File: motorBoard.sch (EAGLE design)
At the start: 8 parts, among them U1 CY8C4247AZI-L485TQFN

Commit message: PRR
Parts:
- removed LED1: (no value), eagle-ltspice:LED_ESML0603
- removed SV1: (no value), con-amp-mt:L05P
- removed SV2: (no value), con-amp-mt:L04P
- added ENCD1, ENCD2, ENCD3, ENCD4: MOLEX5, HuskyRobotics2017-18:MOLEX5
- added LED2: (no value), eagle-ltspice:LED_E
- added LIMIT4A, LIMIT4A1, LIMIT4A2, LIMIT4A3, LIMIT4B, LIMIT4B1, LIMIT4B2, LIMIT4B3, POT1, POT2, POT3, POT4, PWM1, PWM2, PWM3, PWM4: MOLEX3, HuskyRobotics2017-18:MOLEX3
- added U$5: OKI-78SR-3.33SIP, HuskyRobotics2017-18:OKI-78SR-3.33SIP
- added U$6, U$7, U$8, U$9: LEVEL-SHIFTER_NVT2003DPNVT_2003DP_LEVEL_SHIFTER, HuskyRobotics2017-18:LEVEL-SHIFTER_NVT2003DPNVT_2003DP_LEVEL_SHIFTER
- U$2: value OKI-78SR3SIP -> OKI-78SR-53SIP; device HuskyRobotics2017-18:OKI-78SR3SIP -> HuskyRobotics2017-18:OKI-78SR-53SIP
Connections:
- removed net B$10: SV1-1.S, SV1-2.S, SV1-3.S, U1.P3.1, U1.P3.2, U1.P3.3
- removed net B$11: SV2-1.S, SV2-2.S, U1.P3.4, U1.P3.5
- removed net B$2: U1.P0.1, U1.P0.2
- removed net B$6: U1.P1.1, U1.P1.2, U1.P1.3
- removed net B$7: U1.P1.4, U1.P1.5
- removed net B$8: U1.P2.1, U1.P2.2, U1.P2.3
- removed net B$9: U1.P2.4, U1.P2.5
- removed net N$12: SV2-4.S, U$1.VCC, U$2.OUTPUT+, U$3.1A, U$3.2A, U$3.3A, U$3.4A, U$4.OUT_EN, U$4.VCC, U1.VCCD, U1.VDDA@11, U1.VDDA@56, U1.VDDD, U1.VDDIO
- removed net N$13: SV1-4.S, SV1-5.S, SV2-3.S, U$1.GND, U$2.GND, U$4.GND, U1.VSSA@10, U1.VSSA@57, U1.VSSD, U1.VSSIO
- new net +3V3: LIMIT4A.1, LIMIT4A1.1, LIMIT4A2.1, LIMIT4A3.1, LIMIT4B.1, LIMIT4B1.1, LIMIT4B2.1, LIMIT4B3.1, PWM1.1, PWM2.1, PWM3.1, PWM4.1, U$3.1A, U$3.2A, U$3.3A, U$3.4A, U$4.OUT_EN, U$4.VCC, U$5.OUTPUT+, U$6.AREF, U$7.AREF, U$8.AREF, U$9.AREF, U1.VCCD, U1.VDDD, U1.VDDIO
- new net +5V: ENCD1.1, ENCD2.1, ENCD3.1, ENCD4.1, POT1.1, POT2.1, POT3.1, POT4.1, U$2.OUTPUT+, U1.VDDA@11, U1.VDDA@56
- new net GNDA: ENCD1.2, ENCD2.2, ENCD3.2, ENCD4.2, LIMIT4A.2, LIMIT4A1.2, LIMIT4A2.2, LIMIT4A3.2, LIMIT4B.2, LIMIT4B1.2, LIMIT4B2.2, LIMIT4B3.2, POT1.2, POT2.2, POT3.2, POT4.2, PWM1.2, PWM2.2, PWM3.2, PWM4.2, U$2.GND, U$4.GND, U$5.GND, U$6.GND, U$7.GND, U$8.GND, U$9.GND, U1.VSSA@10, U1.VSSA@57, U1.VSSD, U1.VSSIO
- new net N$10: ENCD4.3, U$6.B3
- new net N$11: ENCD4.4, U$6.B2
- new net N$16: ENCD4.5, U$6.B1
- new net N$17: PWM1.3, U1.P2.0
- new net N$18: POT4.3, U1.P3.6
- new net N$19: LIMIT4B.3, U1.P3.5
- new net N$20: LIMIT4A.3, U1.P3.4
- new net N$21: U$7.BREF, U$7.EN
- new net N$22: U$7.A3, U1.P2.1
- new net N$23: U$7.A2, U1.P2.2
- new net N$24: U$7.A1, U1.P2.3
- new net N$25: ENCD1.3, U$7.B3
- new net N$26: ENCD1.4, U$7.B2
- new net N$27: ENCD1.5, U$7.B1
- new net N$28: LIMIT4B1.3, U1.P2.5
- new net N$29: LIMIT4A1.3, U1.P2.4
- new net N$30: POT1.3, U1.P2.6
- new net N$31: PWM2.3, U1.P1.0
- new net N$32: U$8.BREF, U$8.EN
- new net N$33: U$8.A3, U1.P1.1
- new net N$34: U$8.A2, U1.P1.2
- new net N$35: U$8.A1, U1.P1.3
- new net N$36: ENCD2.3, U$8.B3
- new net N$37: ENCD2.4, U$8.B2
- new net N$38: ENCD2.5, U$8.B1
- new net N$39: LIMIT4B2.3, U1.P1.5
- new net N$40: LIMIT4A2.3, U1.P1.4
- new net N$41: POT2.3, U1.P1.6
- new net N$42: PWM3.3, U1.P0.0
- new net N$43: U$9.BREF, U$9.EN
- new net N$44: U$9.A3, U1.P0.1
- new net N$45: U$9.A2, U1.P0.2
- new net N$46: U$9.A1, U1.P0.3
- new net N$47: ENCD3.3, U$9.B3
- new net N$48: ENCD3.4, U$9.B2
- new net N$49: ENCD3.5, U$9.B1
- new net N$50: LIMIT4B3.3, U1.P0.5
- new net N$51: LIMIT4A3.3, U1.P0.4
- new net N$52: POT3.3, U1.P0.6
- net B$4: now also U$3.1B, U$3.4B; no longer U1.P5.1, U1.P5.2
- net N$14: now also U$5.INPUT+
- net N$3: now also U$6.BREF, U$6.EN; no longer U1.P0.0
- net N$4: now also U$3.2B, U1.P5.1; no longer U1.P1.0
- net N$5: now also U$3.3B, U1.P5.2; no longer U1.P2.0
- net N$6: now also PWM4.3
- net N$7: now also U$6.A3, U1.P3.1; no longer U1.P0.5
- net N$8: now also U$6.A2, U1.P3.2; no longer U1.P0.4
- net N$9: now also U$6.A1, U1.P3.3; no longer U1.P0.3
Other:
- note removed: "Each motor has 3 encoder or 1 analog input, 2 limit switches, and 1 pwm output. Analog or Encoder mode is controlled by DIP switch."
- note removed: "LEDs can be connected to some odd GPIOs"
- note removed: "Motor 1 Encoder Inputs"
- note removed: "Motor 1 Limit Switches"
- note removed: "Motor 2 Encoder Inputs"
- note removed: "Motor 2 Limit Switches"
- note removed: "Motor 2 PWM"
- note removed: "Motor 3 Encoder Inputs"
- note removed: "Motor 3 Limit Switches"
- note removed: "Motor 3 PWM"
- note removed: "Motor 4 Encoder Inputs"
- note removed: "Motor 4 Limit Switches"
- note removed: "Motor 4 PWM"
- note removed: "PWM"

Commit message: Minor Tweaks
Added a couple of ground and voltage references.
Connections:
- net +3V3: now also U$1.VCC
- net GNDA: now also U$1.GND
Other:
- moved on the sheet: ENCD4, LIMIT4A, LIMIT4B, POT4, PWM4, U$2, U$5

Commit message: Finishing touches on the schematic
Added indicator LEDs, labeled all nets, spare gpio headers, cleaned up schematic, other misc.  Quickie layout and auto router just for funsies.
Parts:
- removed ENCD1, ENCD2, ENCD3, ENCD4: MOLEX5, HuskyRobotics2017-18:MOLEX5
- removed LIMIT4A, LIMIT4A1, LIMIT4A2, LIMIT4A3, LIMIT4B, LIMIT4B1, LIMIT4B2, LIMIT4B3: MOLEX3, HuskyRobotics2017-18:MOLEX3
- removed U$2: OKI-78SR-53SIP, HuskyRobotics2017-18:OKI-78SR-53SIP
- removed U$5: OKI-78SR-3.33SIP, HuskyRobotics2017-18:OKI-78SR-3.33SIP
- added 1_ENCD3V3, 1_ENCD5V, 2_ENCD3V3, 2_ENCD5V, 3_ENCD3V3, 3_ENCD5V, 4_ENCD3V3, 4_ENCD5V: MOLEX5, HuskyRobotics2017-18:MOLEX5
- added BASIC_HEADER: 2BASIC_HEADER, HuskyRobotics2017-18:2BASIC_HEADER
- added BASIC_HEADER1, BASIC_HEADER2: 6BASIC_HEADER, HuskyRobotics2017-18:6BASIC_HEADER
- added LED1, LED3, LED4, LED5, LED6, LED7, LED8: (no value), eagle-ltspice:LED_E
- added LIMITA1, LIMITA2, LIMITA3, LIMITA4, LIMITB1, LIMITB2, LIMITB3, LIMITB4: MOLEX3, HuskyRobotics2017-18:MOLEX3
- added OKI-78SR-3.3: OKI-78SR-3.33SIP, HuskyRobotics2017-18:OKI-78SR-3.33SIP
- added OKI-78SR-5: OKI-78SR-53SIP, HuskyRobotics2017-18:OKI-78SR-53SIP
- added R1, R2, R3, R4, R5, R6, R7, R8: (no value), eagle-ltspice:RR1206
- added RA, RB, RC, RD: 4.7k, eagle-ltspice:RR1206
- added U$10: SMD4SWSMD4SW, HuskyRobotics2017-18:SMD4SWSMD4SW
- renumbered U$4 to OSCILLATOR_SG-646PCE, U1 to PSOC4200L
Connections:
- net N$1 renamed CANRX
- net N$15 renamed CLK
- net N$2 renamed CANTX
- net N$4 renamed SEL_SW2
- net N$5 renamed SEL_SW3
- removed net B$1: PSOC4200L.P4.1, PSOC4200L.P4.2, PSOC4200L.P4.3, PSOC4200L.P4.4, PSOC4200L.P4.5, PSOC4200L.P4.6
- removed net B$4: PSOC4200L.P5.0, PSOC4200L.P5.3, U$3.1B, U$3.4B
- removed net N$11: ENCD4.4, U$6.B2
- removed net N$14: U$2.INPUT+, U$5.INPUT+
- removed net N$16: ENCD4.5, U$6.B1
- removed net N$18: POT4.3, PSOC4200L.P3.6
- removed net N$19: LIMIT4B.3, PSOC4200L.P3.5
- removed net N$21: U$7.BREF, U$7.EN
- removed net N$22: PSOC4200L.P2.1, U$7.A3
- removed net N$24: PSOC4200L.P2.3, U$7.A1
- removed net N$25: ENCD1.3, U$7.B3
- removed net N$26: ENCD1.4, U$7.B2
- removed net N$27: ENCD1.5, U$7.B1
- removed net N$28: LIMIT4B1.3, PSOC4200L.P2.5
- removed net N$29: LIMIT4A1.3, PSOC4200L.P2.4
- removed net N$3: U$6.BREF, U$6.EN
- removed net N$30: POT1.3, PSOC4200L.P2.6
- removed net N$31: PSOC4200L.P1.0, PWM2.3
- removed net N$32: U$8.BREF, U$8.EN
- removed net N$33: PSOC4200L.P1.1, U$8.A3
- removed net N$34: PSOC4200L.P1.2, U$8.A2
- removed net N$35: PSOC4200L.P1.3, U$8.A1
- removed net N$36: ENCD2.3, U$8.B3
- removed net N$37: ENCD2.4, U$8.B2
- removed net N$38: ENCD2.5, U$8.B1
- removed net N$39: LIMIT4B2.3, PSOC4200L.P1.5
- removed net N$40: LIMIT4A2.3, PSOC4200L.P1.4
- removed net N$41: POT2.3, PSOC4200L.P1.6
- removed net N$42: PSOC4200L.P0.0, PWM3.3
- removed net N$43: U$9.BREF, U$9.EN
- removed net N$44: PSOC4200L.P0.1, U$9.A3
- removed net N$45: PSOC4200L.P0.2, U$9.A2
- removed net N$46: PSOC4200L.P0.3, U$9.A1
- removed net N$47: ENCD3.3, U$9.B3
- removed net N$48: ENCD3.4, U$9.B2
- removed net N$49: ENCD3.5, U$9.B1
- removed net N$50: LIMIT4B3.3, PSOC4200L.P0.5
- removed net N$51: LIMIT4A3.3, PSOC4200L.P0.4
- removed net N$52: POT3.3, PSOC4200L.P0.6
- removed net N$6: PSOC4200L.P3.0, PWM4.3
- removed net N$8: PSOC4200L.P3.2, U$6.A2
- removed net N$9: PSOC4200L.P3.3, U$6.A1
- new net +24V: LED1.A, OKI-78SR-3.3.INPUT+, OKI-78SR-5.INPUT+
- new net BASIC_HEADER1-1: BASIC_HEADER1.1, PSOC4200L.P4.1
- new net BASIC_HEADER1-2: BASIC_HEADER1.2, PSOC4200L.P4.2
- new net BASIC_HEADER1-3: BASIC_HEADER1.3, PSOC4200L.P4.3
- new net BASIC_HEADER1-4: BASIC_HEADER1.4, PSOC4200L.P4.4
- new net BASIC_HEADER1-5: BASIC_HEADER1.5, PSOC4200L.P4.5
- new net BASIC_HEADER1-6: BASIC_HEADER1.6, PSOC4200L.P4.6
- new net BASIC_HEADER2-1: BASIC_HEADER2.1, PSOC4200L.P5.5
- new net BASIC_HEADER2-2: BASIC_HEADER2.2, PSOC4200L.P6.0
- new net BASIC_HEADER2-3: BASIC_HEADER2.3, PSOC4200L.P6.4/P12.0
- new net BASIC_HEADER2-4: BASIC_HEADER2.4, PSOC4200L.P6.5/P12.1
- new net BASIC_HEADER2-5: BASIC_HEADER2.5, PSOC4200L.P7.0
- new net BASIC_HEADER2-6: BASIC_HEADER2.6, PSOC4200L.P7.1
- new net CANH: U$1.CANH
- new net CANL: U$1.CANL
- new net LED4: LED4.A, PSOC4200L.P1.7/VREF
- new net LED5: LED5.A, PSOC4200L.P0.7
- new net LED6: LED6.A, PSOC4200L.P4.0
- new net LED7: LED7.A, PSOC4200L.D-/P13.1
- new net LED8: LED8.A, PSOC4200L.VBUS/P13.2
- new net LEVEL_SHIFT_EN1: RD.2, U$10.1B, U$8.EN
- new net LEVEL_SHIFT_EN2: RC.2, U$10.2B, U$7.EN
- new net LEVEL_SHIFT_EN3: RB.2, U$10.3B, U$6.EN
- new net LEVEL_SHIFT_EN4: RA.2, U$10.4B, U$9.EN
- new net MOTOR1A1: 1_ENCD3V3.4, PSOC4200L.P0.2, U$8.A1
- new net MOTOR1A2: 1_ENCD3V3.3, PSOC4200L.P0.1, U$8.A2
- new net MOTOR1A3: 1_ENCD3V3.2, PSOC4200L.P0.0, U$8.A3
- new net MOTOR1B1: 1_ENCD5V.4, U$8.B1
- new net MOTOR1B2: 1_ENCD5V.3, U$8.B2
- new net MOTOR1B3: 1_ENCD5V.2, U$8.B3
- new net MOTOR1LIMA: LIMITA1.2, PSOC4200L.P0.3
- new net MOTOR1LIMB: LIMITB1.2, PSOC4200L.P0.4
- new net MOTOR1POT: POT1.2, PSOC4200L.P0.6
- new net MOTOR1PWM: PSOC4200L.P0.5, PWM1.2
- new net MOTOR2A1: 2_ENCD3V3.4, PSOC4200L.P1.2, U$7.A1
- new net MOTOR2A2: 2_ENCD3V3.3, PSOC4200L.P1.1, U$7.A2
- new net MOTOR2A3: 2_ENCD3V3.2, PSOC4200L.P1.0, U$7.A3
- new net MOTOR2B1: 2_ENCD5V.4, U$7.B1
- new net MOTOR2B2: 2_ENCD5V.3, U$7.B2
- new net MOTOR2B3: 2_ENCD5V.2, U$7.B3
- new net MOTOR2LIMA: LIMITA2.2, PSOC4200L.P1.3
- new net MOTOR2LIMB: LIMITB2.2, PSOC4200L.P1.4
- new net MOTOR2POT: POT2.2, PSOC4200L.P1.6
- new net MOTOR2PWM: PSOC4200L.P1.5, PWM2.2
- new net MOTOR3A1: 3_ENCD3V3.4, PSOC4200L.P2.2, U$6.A1
- new net MOTOR3A2: 3_ENCD3V3.3, PSOC4200L.P2.1, U$6.A2
- new net MOTOR3A3: 3_ENCD3V3.2, PSOC4200L.P2.0, U$6.A3
- new net MOTOR3B1: 3_ENCD5V.4, U$6.B1
- new net MOTOR3B2: 3_ENCD5V.3, U$6.B2
- new net MOTOR3B3: 3_ENCD5V.2, U$6.B3
- new net MOTOR3LIMA: LIMITA3.2, PSOC4200L.P2.3
- new net MOTOR3LIMB: LIMITB3.2, PSOC4200L.P2.4
- new net MOTOR3POT: POT3.2, PSOC4200L.P2.6
- new net MOTOR3PWM: PSOC4200L.P2.5, PWM3.2
- new net MOTOR4A1: 4_ENCD3V3.4, PSOC4200L.P3.1, U$9.A1
- new net MOTOR4A2: 4_ENCD3V3.3, PSOC4200L.P3.0, U$9.A2
- new net MOTOR4A3: 4_ENCD3V3.2, PSOC4200L.P2.7, U$9.A3
- new net MOTOR4B1: 4_ENCD5V.4, U$9.B1
- new net MOTOR4B2: 4_ENCD5V.3, U$9.B2
- new net MOTOR4B3: 4_ENCD5V.2, U$9.B3
- new net MOTOR4LIMA: LIMITA4.2, PSOC4200L.P3.4
- new net MOTOR4LIMB: LIMITB4.2, PSOC4200L.P3.5
- new net MOTOR4POT4: POT4.2, PSOC4200L.P3.7
- new net MOTOR4PWM: PSOC4200L.P3.6, PWM4.2
- new net N$1: LED1.C, R1.2
- new net N$13: LED5.C, R5.2
- new net N$4: LED2.C, R2.2
- new net SEL_SW1: PSOC4200L.P5.0, U$3.1B
- new net SEL_SW4: PSOC4200L.P5.3, U$3.4B
- new net SWD_CLK: BASIC_HEADER.2, PSOC4200L.P3.3
- new net SWD_DATA: BASIC_HEADER.1, PSOC4200L.P3.2
- net +3V3: now also 1_ENCD3V3.1, 2_ENCD3V3.1, 3_ENCD3V3.1, 4_ENCD3V3.1, LED3.A, LIMITA1.1, LIMITA2.1, LIMITA3.1, LIMITA4.1, LIMITB1.1, LIMITB2.1, LIMITB3.1, LIMITB4.1, OKI-78SR-3.3.OUTPUT+, POT1.1, POT2.1, POT3.1, POT4.1, U$10.1A, U$10.2A, U$10.3A, U$10.4A; no longer LIMIT4A.1, LIMIT4A1.1, LIMIT4A2.1, LIMIT4A3.1, LIMIT4B.1, LIMIT4B1.1, LIMIT4B2.1, LIMIT4B3.1, U$5.OUTPUT+
- net +5V: now also 1_ENCD5V.1, 2_ENCD5V.1, 3_ENCD5V.1, 4_ENCD5V.1, LED2.A, OKI-78SR-5.OUTPUT+, U$6.BREF, U$7.BREF, U$8.BREF, U$9.BREF; no longer ENCD1.1, ENCD2.1, ENCD3.1, ENCD4.1, POT1.1, POT2.1, POT3.1, POT4.1, U$2.OUTPUT+
- net GNDA: now also 1_ENCD3V3.5, 1_ENCD5V.5, 2_ENCD3V3.5, 2_ENCD5V.5, 3_ENCD3V3.5, 3_ENCD5V.5, 4_ENCD3V3.5, 4_ENCD5V.5, LIMITA1.3, LIMITA2.3, LIMITA3.3, LIMITA4.3, LIMITB1.3, LIMITB2.3, LIMITB3.3, LIMITB4.3, OKI-78SR-3.3.GND, OKI-78SR-5.GND, POT1.3, POT2.3, POT3.3, POT4.3, PWM1.3, PWM2.3, PWM3.3, PWM4.3, R1.1, R2.1, R3.1, R4.1, R5.1, R6.1, R7.1, R8.1, RA.1, RB.1, RC.1, RD.1; no longer ENCD1.2, ENCD2.2, ENCD3.2, ENCD4.2, LIMIT4A.2, LIMIT4A1.2, LIMIT4A2.2, LIMIT4A3.2, LIMIT4B.2, LIMIT4B1.2, LIMIT4B2.2, LIMIT4B3.2, POT1.2, POT2.2, POT3.2, POT4.2, PWM1.2, PWM2.2, PWM3.2, PWM4.2, U$2.GND, U$5.GND
- net N$10: now also LED4.C, R4.2; no longer ENCD4.3, U$6.B3
- net N$17: now also LED6.C, R6.2; no longer PSOC4200L.P2.0, PWM1.3
- net N$20: now also LED7.C, R7.2; no longer LIMIT4A.3, PSOC4200L.P3.4
- net N$23: now also LED8.C, R8.2; no longer PSOC4200L.P2.2, U$7.A2
- net N$7: now also LED3.C, R3.2; no longer PSOC4200L.P3.1, U$6.A3
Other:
- note added: "Motor1"
- note added: "Motor2"
- note added: "Motor3"
- note added: "Motor4"
- note added: "Need resistor Values!"
- note added: "Program/Debug Header!"
- note removed: "24V Rail"
- note removed: "JTAG"

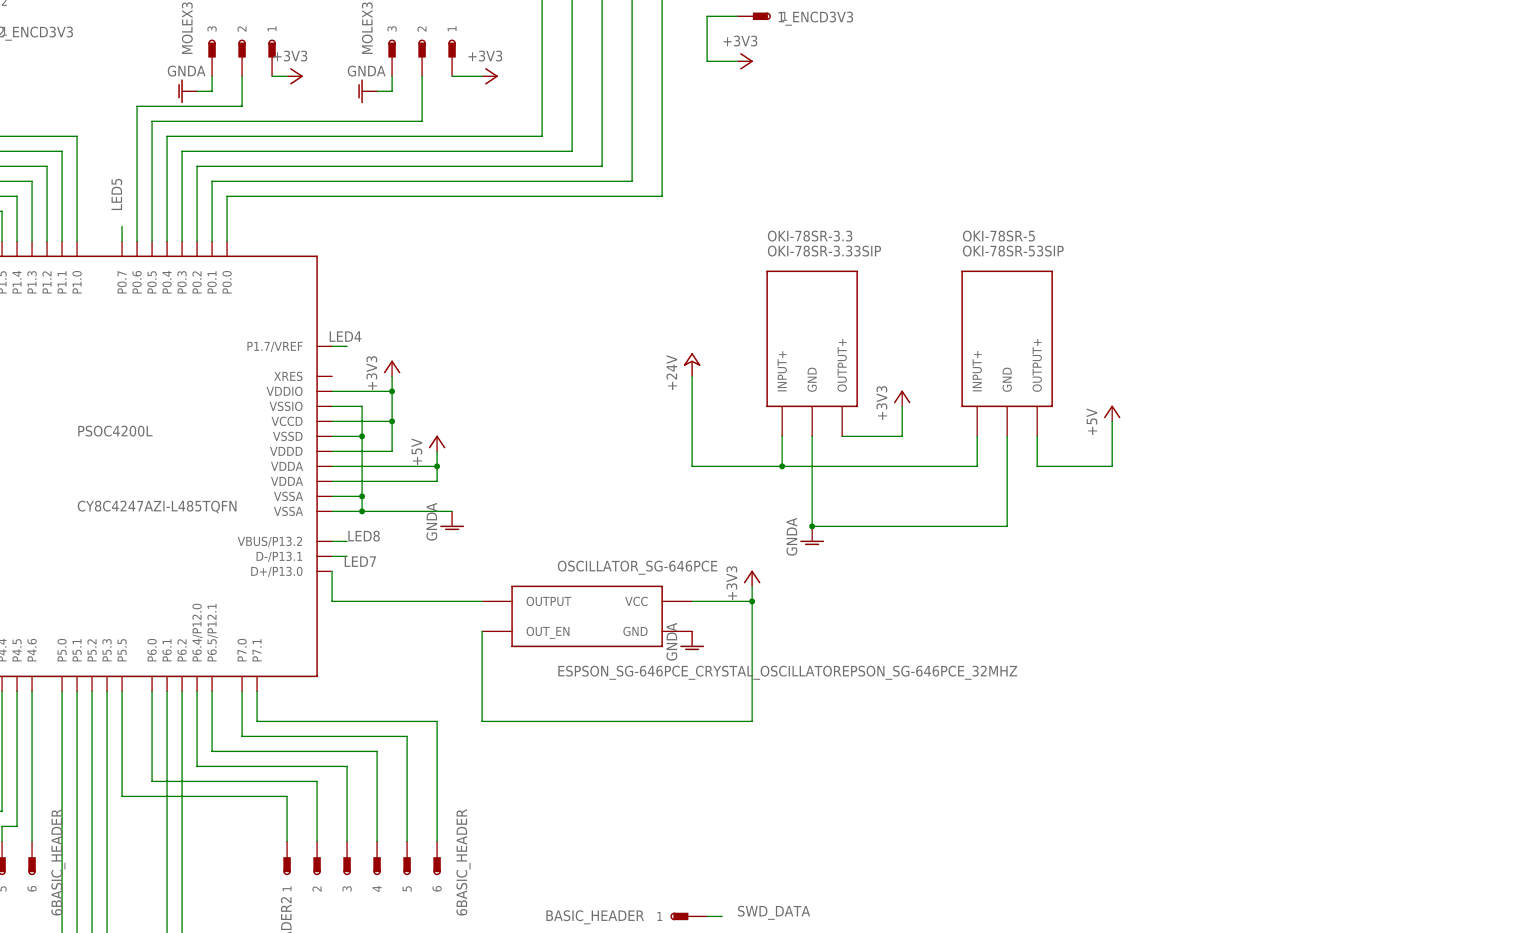
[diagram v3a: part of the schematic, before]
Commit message: Change CLK_EXT pin
Had to move LED5, Motor1LimitSwitch as well.
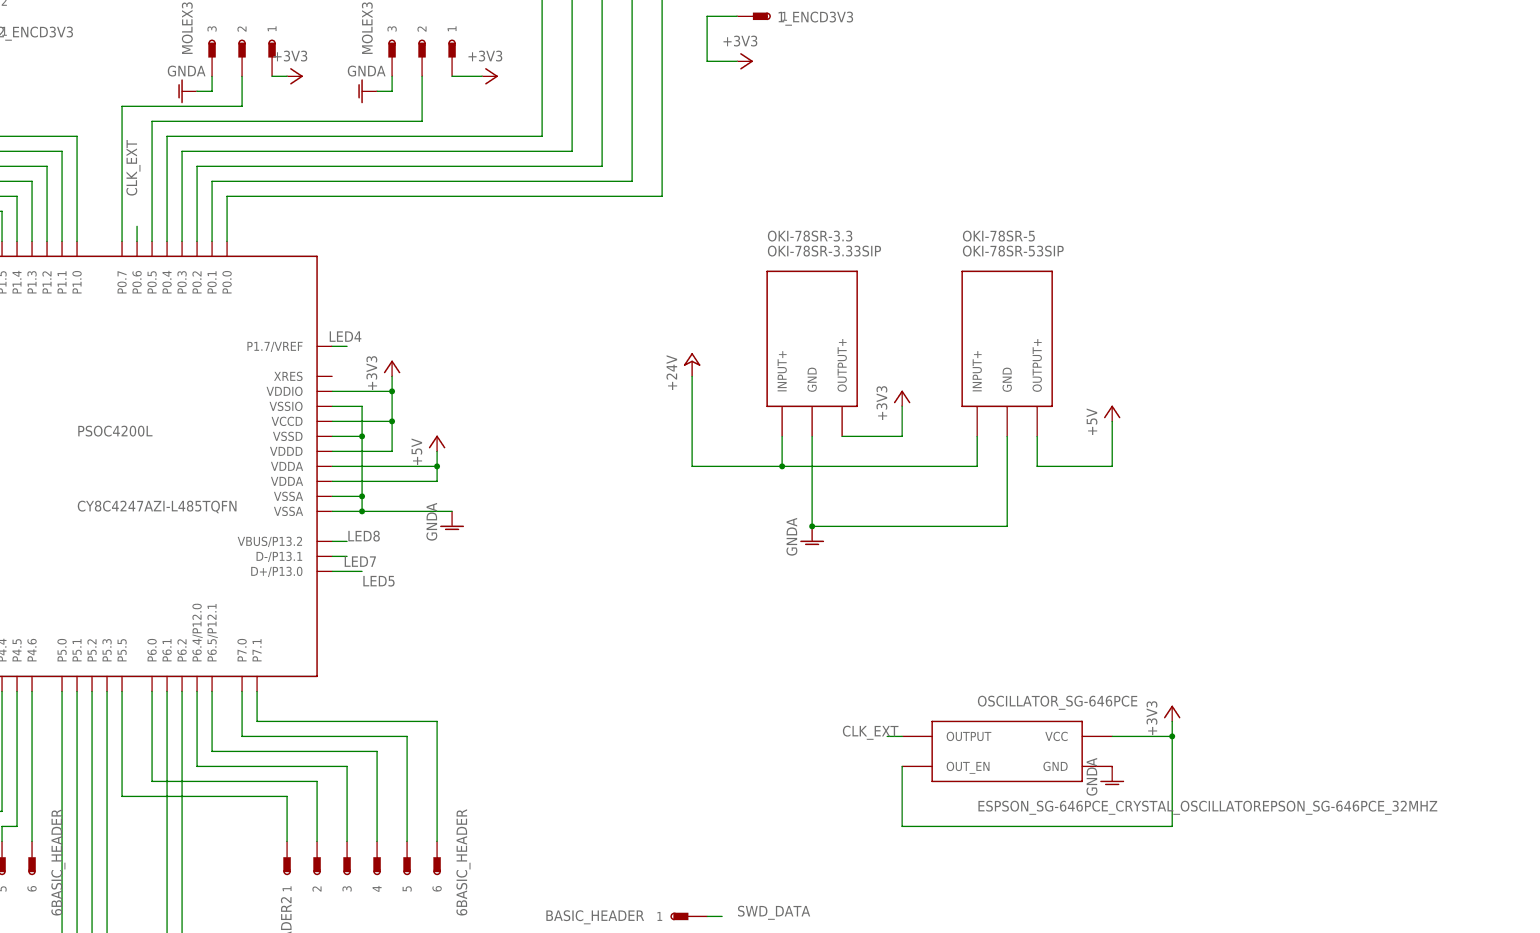
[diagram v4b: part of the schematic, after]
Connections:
- removed net CLK: OSCILLATOR_SG-646PCE.OUTPUT, PSOC4200L.D+/P13.0
- new net CLK_EXT: OSCILLATOR_SG-646PCE.OUTPUT, PSOC4200L.P0.6
- net LED5: now also PSOC4200L.D+/P13.0; no longer PSOC4200L.P0.7
- net MOTOR1POT: now also PSOC4200L.P0.7; no longer PSOC4200L.P0.6
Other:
- moved on the sheet: OSCILLATOR_SG-646PCE
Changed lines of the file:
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@@
 <instance part="U$1" gate="G$1" x="50.8" y="-114.3"/>
 <instance part="U$3" gate="G$1" x="-2.54" y="-106.68" rot="R90"/>
-<instance part="OSCILLATOR_SG-646PCE" gate="G$1" x="81.28" y="-25.4"/>
+<instance part="OSCILLATOR_SG-646PCE" gate="G$1" x="152.4" y="-48.26"/>
 <instance part="LED1" gate="G$1" x="114.3" y="-114.3"/>
 <instance part="OKI-78SR-3.3" gate="G$1" x="124.46" y="12.7"/>
@@
 <instance part="+3V14" gate="G$1" x="134.62" y="12.7"/>
 <instance part="P+13" gate="1" x="170.18" y="10.16"/>
-<instance part="+3V15" gate="G$1" x="109.22" y="-17.78"/>
-<instance part="GND26" gate="1" x="99.06" y="-30.48"/>
+<instance part="+3V15" gate="G$1" x="180.34" y="-40.64"/>
+<instance part="GND26" gate="1" x="170.18" y="-53.34"/>
 <instance part="+3V16" gate="G$1" x="48.26" y="17.78"/>
 <instance part="GND27" gate="1" x="58.42" y="-10.16"/>
@@
 </segment>
 </net>
-<net name="CLK" class="0">
-<segment>
-<pinref part="PSOC4200L" gate="G$1" pin="D+/P13.0"/>
-<wire x1="63.5" y1="-22.86" x2="38.1" y2="-22.86" width="0.1524" layer="91"/>
-<wire x1="38.1" y1="-22.86" x2="38.1" y2="-17.78" width="0.1524" layer="91"/>
-<pinref part="OSCILLATOR_SG-646PCE" gate="G$1" pin="OUTPUT"/>
-</segment>
-</net>
 <net name="CANRX" class="0">
 <segment>
@@
 <segment>
 <pinref part="+3V15" gate="G$1" pin="+3V3"/>
-<wire x1="109.22" y1="-22.86" x2="109.22" y2="-20.32" width="0.1524" layer="91"/>
+<wire x1="180.34" y1="-45.72" x2="180.34" y2="-43.18" width="0.1524" layer="91"/>
 <pinref part="OSCILLATOR_SG-646PCE" gate="G$1" pin="VCC"/>
-<wire x1="99.06" y1="-22.86" x2="109.22" y2="-22.86" width="0.1524" layer="91"/>
+<wire x1="170.18" y1="-45.72" x2="180.34" y2="-45.72" width="0.1524" layer="91"/>
 <pinref part="OSCILLATOR_SG-646PCE" gate="G$1" pin="OUT_EN"/>
-<wire x1="63.5" y1="-27.94" x2="63.5" y2="-43.18" width="0.1524" layer="91"/>
-<wire x1="63.5" y1="-43.18" x2="109.22" y2="-43.18" width="0.1524" layer="91"/>
-<wire x1="109.22" y1="-22.86" x2="109.22" y2="-43.18" width="0.1524" layer="91"/>
-<junction x="109.22" y="-22.86"/>
+<wire x1="134.62" y1="-50.8" x2="134.62" y2="-60.96" width="0.1524" layer="91"/>
+<wire x1="134.62" y1="-60.96" x2="180.34" y2="-60.96" width="0.1524" layer="91"/>
+<wire x1="180.34" y1="-45.72" x2="180.34" y2="-60.96" width="0.1524" layer="91"/>
+<junction x="180.34" y="-45.72"/>
 </segment>
 <segment>
@@
 <pinref part="POT1" gate="G$1" pin="2"/>
 <wire x1="22.86" y1="66.04" x2="22.86" y2="60.96" width="0.1524" layer="91"/>
-<wire x1="22.86" y1="60.96" x2="5.08" y2="60.96" width="0.1524" layer="91"/>
-<wire x1="5.08" y1="60.96" x2="5.08" y2="38.1" width="0.1524" layer="91"/>
-<pinref part="PSOC4200L" gate="G$1" pin="P0.6"/>
+<wire x1="22.86" y1="60.96" x2="2.54" y2="60.96" width="0.1524" layer="91"/>
+<pinref part="PSOC4200L" gate="G$1" pin="P0.7"/>
+<wire x1="2.54" y1="60.96" x2="2.54" y2="38.1" width="0.1524" layer="91"/>
 </segment>
 </net>
@@
 <net name="LED5" class="0">
 <segment>
-<pinref part="PSOC4200L" gate="G$1" pin="P0.7"/>
-<wire x1="2.54" y1="38.1" x2="2.54" y2="40.64" width="0.1524" layer="91"/>
-<label x="2.54" y="43.18" size="1.778" layer="95" rot="R90"/>
-</segment>
-<segment>
 <pinref part="LED5" gate="G$1" pin="A"/>
 <wire x1="157.48" y1="-111.76" x2="157.48" y2="-109.22" width="0.1524" layer="91"/>
 <label x="157.48" y="-106.68" size="1.778" layer="95"/>
 </segment>
+<segment>
+<pinref part="PSOC4200L" gate="G$1" pin="D+/P13.0"/>
+<wire x1="38.1" y1="-17.78" x2="43.18" y2="-17.78" width="0.1524" layer="91"/>
+<label x="43.18" y="-20.32" size="1.778" layer="95"/>
+</segment>
 </net>
 <net name="LED8" class="0">
@@
 </segment>
 </net>
+<net name="CLK_EXT" class="0">
+<segment>
+<pinref part="PSOC4200L" gate="G$1" pin="P0.6"/>
+<wire x1="5.08" y1="38.1" x2="5.08" y2="40.64" width="0.1524" layer="91"/>
+<label x="5.08" y="45.72" size="1.778" layer="95" rot="R90"/>
+</segment>
+<segment>
+<wire x1="134.62" y1="-45.72" x2="132.08" y2="-45.72" width="0.1524" layer="91"/>
+<pinref part="OSCILLATOR_SG-646PCE" gate="G$1" pin="OUTPUT"/>
+<label x="124.46" y="-45.72" size="1.778" layer="95"/>
+</segment>
+</net>
